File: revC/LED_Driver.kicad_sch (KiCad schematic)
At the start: 26 parts, among them Q1 BC857AW,115, Q2 BC857AW,115, Q3 BC857AW,115, Q602 BC857AW,115

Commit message: updated layout for fm.
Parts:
- removed Q1, Q3, Q602: BC857AW,115, Package_TO_SOT_SMD:SOT-323_SC-70, symbol backplane-rescue:Q_PNP_BEC-Device
- removed R1, R604: 0R, Resistor_SMD:R_0402_1005Metric, symbol backplane-rescue:R_US-Device
- removed R2, R3, R5: 4.7k, Resistor_SMD:R_0402_1005Metric, symbol backplane-rescue:R_US-Device
- added F1: 500mA, Fuse:Fuse_0603_1608Metric, symbol Device:Fuse_Small
- added R10, R11, R12, R13, R6, R7, R8, R9: 1k, Resistor_SMD:R_0402_1005Metric, symbol backplane-rescue:R_US-Device
- added R14, R15: 0R, Resistor_SMD:R_0402_1005Metric, symbol backplane-rescue:R_US-Device
- C201, C202, C203, C204, C205, C206, C207, C208: value 1uF -> 0.1uF; footprint Capacitor_SMD:C_0603_1608Metric -> Capacitor_SMD:C_0402_1005Metric
- D201, D202, D203, D204, D205, D206, D207, D208: value SK68XX-EC3210R -> SK6805-EC321R; footprint CubeSat_Backplane:SK6812-EC3210F -> CubeSat_Backplane:SK68xx-EC120x_ReverseMount; symbol CubeSat_Backplane:SK6812-EC321F -> CubeSat_Backplane:SK68xx
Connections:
- net DIN: now also R14.2
- net DIN_LED: now also R14.1, R6.2; no longer D208.3 (DIN)
- net DOUT: now also R15.1
- net DOUT_LED: now also R15.2
- net LED_PWR: now also F1.2; no longer Q2.2 (E)
- net at D201.3 (DIN): now also R13.2; no longer D202.2 (DOUT)
- net at D208.2 (DOUT): now also R7.1; no longer D207.3 (DIN)
- net at D202.3 (DIN): now also R12.2; no longer D203.2 (DOUT)
- net at D204.2 (DOUT): now also R11.1; no longer D203.3 (DIN)
- net at D204.3 (DIN): now also R10.2; no longer D205.2 (DOUT)
- net at D206.2 (DOUT): now also R9.1; no longer D205.3 (DIN)
- net at D207.2 (DOUT): now also R8.1; no longer D206.3 (DIN)
- new net: D208.3 (DIN), R6.1
- new net: F1.1, Q2.2 (E)
- new net: D206.3 (DIN), R8.2
- new net: D202.2 (DOUT), R13.1
- new net: D205.3 (DIN), R9.2
- new net: D205.2 (DOUT), R10.1
- new net: D203.2 (DOUT), R12.1
- new net: D207.3 (DIN), R7.2
- new net: D203.3 (DIN), R11.2
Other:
- note added: "LED power sw"
- note added: "Reverse-Mounted Addressable RGB LEDs (Neopixels)"
- note removed: "Din, Dout Protection Buffer"
- note removed: "LED power buffer"
- note removed: "Reverse-Mounted NeoPixels"
- moved on the sheet: C201, C202, C203, C204, C205, C206, C207, C208

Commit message: removed old files
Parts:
- renumbered F1 to F200, Q2 to Q200, R4 to R200, R14 to R201, R15 to R202, R13 to R203, R12 to R204, R11 to R205, R10 to R206, R9 to R207, R8 to R208, R7 to R209, R6 to R210
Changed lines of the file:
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@@
   (symbol (lib_id "backplane-rescue:Q_PNP_BEC-Device") (at 62.865 49.53 270) (mirror x) (unit 1)
     (in_bom yes) (on_board yes) (dnp no)
-    (property "Reference" "Q2" (at 70.485 50.165 90)
+    (property "Reference" "Q200" (at 70.485 50.165 90)
       (effects (font (size 1.27 1.27)))
     )
@@
       (project "backplane"
         (path "/83db9fc1-2403-4316-a6ed-41bf80609364/00000000-0000-0000-0000-000061b9d717"
-          (reference "Q2") (unit 1)
+          (reference "Q200") (unit 1)
         )
       )
@@
   (symbol (lib_name "R_US-Device_1") (lib_id "backplane-rescue:R_US-Device") (at 181.61 63.5 90) (unit 1)
     (in_bom yes) (on_board yes) (dnp no)
-    (property "Reference" "R8" (at 177.8 62.23 90)
+    (property "Reference" "R208" (at 177.8 62.23 90)
       (effects (font (size 1.27 1.27)))
     )
@@
       (project "backplane"
         (path "/83db9fc1-2403-4316-a6ed-41bf80609364/00000000-0000-0000-0000-000061b9d717"
-          (reference "R8") (unit 1)
+          (reference "R208") (unit 1)
         )
       )
@@
   (symbol (lib_name "R_US-Device_1") (lib_id "backplane-rescue:R_US-Device") (at 213.36 63.5 90) (unit 1)
     (in_bom yes) (on_board yes) (dnp no)
-    (property "Reference" "R9" (at 209.55 62.23 90)
+    (property "Reference" "R207" (at 209.55 62.23 90)
       (effects (font (size 1.27 1.27)))
     )
@@
       (project "backplane"
         (path "/83db9fc1-2403-4316-a6ed-41bf80609364/00000000-0000-0000-0000-000061b9d717"
-          (reference "R9") (unit 1)
+          (reference "R207") (unit 1)
         )
       )
@@
   (symbol (lib_name "R_US-Device_1") (lib_id "backplane-rescue:R_US-Device") (at 181.61 101.6 90) (unit 1)
     (in_bom yes) (on_board yes) (dnp no)
-    (property "Reference" "R12" (at 177.8 100.33 90)
+    (property "Reference" "R204" (at 177.8 100.33 90)
       (effects (font (size 1.27 1.27)))
     )
@@
       (project "backplane"
         (path "/83db9fc1-2403-4316-a6ed-41bf80609364/00000000-0000-0000-0000-000061b9d717"
-          (reference "R12") (unit 1)
+          (reference "R204") (unit 1)
         )
       )
@@
   (symbol (lib_id "backplane-rescue:R_US-Device") (at 55.88 74.93 270) (unit 1)
     (in_bom yes) (on_board yes) (dnp no)
-    (property "Reference" "R14" (at 55.88 69.723 90)
+    (property "Reference" "R201" (at 55.88 69.723 90)
       (effects (font (size 1.27 1.27)))
     )
@@
       (project "backplane"
         (path "/83db9fc1-2403-4316-a6ed-41bf80609364/00000000-0000-0000-0000-000061b9d717"
-          (reference "R14") (unit 1)
+          (reference "R201") (unit 1)
         )
       )
@@
   (symbol (lib_id "backplane-rescue:R_US-Device") (at 47.625 59.69 90) (unit 1)
     (in_bom yes) (on_board yes) (dnp no)
-    (property "Reference" "R4" (at 45.085 60.96 90)
+    (property "Reference" "R200" (at 45.085 60.96 90)
       (effects (font (size 1.27 1.27)) (justify left))
     )
@@
       (project "backplane"
         (path "/83db9fc1-2403-4316-a6ed-41bf80609364/00000000-0000-0000-0000-000061b9d717"
-          (reference "R4") (unit 1)
+          (reference "R200") (unit 1)
         )
       )
@@
   (symbol (lib_name "R_US-Device_1") (lib_id "backplane-rescue:R_US-Device") (at 149.86 63.5 90) (unit 1)
     (in_bom yes) (on_board yes) (dnp no)
-    (property "Reference" "R7" (at 146.05 62.23 90)
+    (property "Reference" "R209" (at 146.05 62.23 90)
       (effects (font (size 1.27 1.27)))
     )
@@
       (project "backplane"
         (path "/83db9fc1-2403-4316-a6ed-41bf80609364/00000000-0000-0000-0000-000061b9d717"
-          (reference "R7") (unit 1)
+          (reference "R209") (unit 1)
         )
       )
@@
   (symbol (lib_name "R_US-Device_1") (lib_id "backplane-rescue:R_US-Device") (at 149.86 101.6 90) (unit 1)
     (in_bom yes) (on_board yes) (dnp no)
-    (property "Reference" "R11" (at 146.05 100.33 90)
+    (property "Reference" "R205" (at 146.05 100.33 90)
       (effects (font (size 1.27 1.27)))
     )
@@
       (project "backplane"
         (path "/83db9fc1-2403-4316-a6ed-41bf80609364/00000000-0000-0000-0000-000061b9d717"
-          (reference "R11") (unit 1)
+          (reference "R205") (unit 1)
         )
       )
@@
   (symbol (lib_name "R_US-Device_1") (lib_id "backplane-rescue:R_US-Device") (at 113.03 63.5 270) (mirror x) (unit 1)
     (in_bom yes) (on_board yes) (dnp no)
-    (property "Reference" "R6" (at 116.84 62.23 90)
+    (property "Reference" "R210" (at 116.84 62.23 90)
       (effects (font (size 1.27 1.27)))
     )
@@
       (project "backplane"
         (path "/83db9fc1-2403-4316-a6ed-41bf80609364/00000000-0000-0000-0000-000061b9d717"
-          (reference "R6") (unit 1)
+          (reference "R210") (unit 1)
         )
       )
@@
   (symbol (lib_name "R_US-Device_1") (lib_id "backplane-rescue:R_US-Device") (at 213.36 101.6 90) (unit 1)
     (in_bom yes) (on_board yes) (dnp no)
-    (property "Reference" "R13" (at 209.55 100.33 90)
+    (property "Reference" "R203" (at 209.55 100.33 90)
       (effects (font (size 1.27 1.27)))
     )
@@
       (project "backplane"
         (path "/83db9fc1-2403-4316-a6ed-41bf80609364/00000000-0000-0000-0000-000061b9d717"
-          (reference "R13") (unit 1)
+          (reference "R203") (unit 1)
         )
       )
@@
   (symbol (lib_name "R_US-Device_1") (lib_id "backplane-rescue:R_US-Device") (at 119.38 101.6 90) (unit 1)
     (in_bom yes) (on_board yes) (dnp no)
-    (property "Reference" "R10" (at 115.57 100.33 90)
+    (property "Reference" "R206" (at 115.57 100.33 90)
       (effects (font (size 1.27 1.27)))
     )
@@
       (project "backplane"
         (path "/83db9fc1-2403-4316-a6ed-41bf80609364/00000000-0000-0000-0000-000061b9d717"
-          (reference "R10") (unit 1)
+          (reference "R206") (unit 1)
         )
       )
@@
   (symbol (lib_id "backplane-rescue:R_US-Device") (at 55.88 83.82 270) (unit 1)
     (in_bom yes) (on_board yes) (dnp no)
-    (property "Reference" "R15" (at 55.88 78.613 90)
+    (property "Reference" "R202" (at 55.88 78.613 90)
       (effects (font (size 1.27 1.27)))
     )
@@
       (project "backplane"
         (path "/83db9fc1-2403-4316-a6ed-41bf80609364/00000000-0000-0000-0000-000061b9d717"
-          (reference "R15") (unit 1)
+          (reference "R202") (unit 1)
         )
       )
@@
   (symbol (lib_id "Device:Fuse_Small") (at 48.26 46.99 180) (unit 1)
     (in_bom yes) (on_board yes) (dnp no)
-    (property "Reference" "F1" (at 49.53 49.53 90)
-      (effects (font (size 1.27 1.27)) (justify left))
-    )
-    (property "Value" "500mA" (at 49.53 40.005 90)
+    (property "Reference" "F200" (at 46.99 43.18 0)
+      (effects (font (size 1.27 1.27)) (justify left))
+    )
+    (property "Value" "500mA" (at 48.26 45.72 0)
       (effects (font (size 1.27 1.27)) (justify left))
     )
@@
       (project "backplane"
         (path "/83db9fc1-2403-4316-a6ed-41bf80609364/00000000-0000-0000-0000-000061b9d717"
-          (reference "F1") (unit 1)
-        )
-      )
+          (reference "F200") (unit 1)
+        )
+      )

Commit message: working post-review changes
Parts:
- removed F200: 500mA, Fuse:Fuse_0603_1608Metric, symbol Device:Fuse_Small
- removed Q200: BC857AW,115, Package_TO_SOT_SMD:SOT-323_SC-70, symbol backplane-rescue:Q_PNP_BEC-Device
- removed R200: 4.7k, Resistor_SMD:R_0402_1005Metric, symbol backplane-rescue:R_US-Device
- removed R201, R202: 0R, Resistor_SMD:R_0402_1005Metric, symbol backplane-rescue:R_US-Device
- D201, D202, D203, D204, D205, D206, D207, D208: Manufacturer Part Number 1 (none) -> SK6812-EC321R
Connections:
- net DIN_LED is gone; now on net DIN: R210.2
- net DOUT_LED is gone; now on net DOUT: D201.2 (DOUT)
- net LED_Vcc is gone; now on net LED_PWR: C201.1, C202.1, C203.1, C204.1, C205.1, C206.1, C207.1, C208.1, D201.4 (VDD), D202.4 (VDD), D203.4 (VDD), D204.4 (VDD), D205.4 (VDD), D206.4 (VDD), D207.4 (VDD), D208.4 (VDD)
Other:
- note removed: "LED power sw"

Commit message: revC commit
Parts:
- D201, D202, D203, D204, D205, D206, D207, D208: value SK6805-EC321R -> SK6805-EC321F; footprint CubeSat_Backplane:SK68xx-EC120x_ReverseMount -> SierraLobo:SK68xx-EC120x_ReverseMount
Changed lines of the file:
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@@
       (effects (font (size 1.27 1.27)))
     )
-    (property "Value" "SK6805-EC321R" (at 213.36 106.1593 0)
-      (effects (font (size 1.27 1.27)))
-    )
-    (property "Footprint" "CubeSat_Backplane:SK68xx-EC120x_ReverseMount" (at 228.6 109.22 0)
+    (property "Value" "SK6805-EC321F" (at 213.36 106.1593 0)
+      (effects (font (size 1.27 1.27)))
+    )
+    (property "Footprint" "SierraLobo:SK68xx-EC120x_ReverseMount" (at 228.6 109.22 0)
       (effects (font (size 1.27 1.27)) (justify left top) hide)
     )
@@
       (effects (font (size 1.27 1.27)))
     )
-    (property "Value" "SK6805-EC321R" (at 119.38 68.0593 0)
-      (effects (font (size 1.27 1.27)))
-    )
-    (property "Footprint" "CubeSat_Backplane:SK68xx-EC120x_ReverseMount" (at 134.62 71.12 0)
+    (property "Value" "SK6805-EC321F" (at 119.38 68.0593 0)
+      (effects (font (size 1.27 1.27)))
+    )
+    (property "Footprint" "SierraLobo:SK68xx-EC120x_ReverseMount" (at 134.62 71.12 0)
       (effects (font (size 1.27 1.27)) (justify left top) hide)
     )
@@
       (effects (font (size 1.27 1.27)))
     )
-    (property "Value" "SK6805-EC321R" (at 181.61 106.1593 0)
-      (effects (font (size 1.27 1.27)))
-    )
-    (property "Footprint" "CubeSat_Backplane:SK68xx-EC120x_ReverseMount" (at 196.85 109.22 0)
+    (property "Value" "SK6805-EC321F" (at 181.61 106.1593 0)
+      (effects (font (size 1.27 1.27)))
+    )
+    (property "Footprint" "SierraLobo:SK68xx-EC120x_ReverseMount" (at 196.85 109.22 0)
       (effects (font (size 1.27 1.27)) (justify left top) hide)
     )
@@
       (effects (font (size 1.27 1.27)))
     )
-    (property "Value" "SK6805-EC321R" (at 119.38 106.1593 0)
-      (effects (font (size 1.27 1.27)))
-    )
-    (property "Footprint" "CubeSat_Backplane:SK68xx-EC120x_ReverseMount" (at 134.62 109.22 0)
+    (property "Value" "SK6805-EC321F" (at 119.38 106.1593 0)
+      (effects (font (size 1.27 1.27)))
+    )
+    (property "Footprint" "SierraLobo:SK68xx-EC120x_ReverseMount" (at 134.62 109.22 0)
       (effects (font (size 1.27 1.27)) (justify left top) hide)
     )
@@
       (effects (font (size 1.27 1.27)))
     )
-    (property "Value" "SK6805-EC321R" (at 213.36 68.0593 0)
-      (effects (font (size 1.27 1.27)))
-    )
-    (property "Footprint" "CubeSat_Backplane:SK68xx-EC120x_ReverseMount" (at 228.6 71.12 0)
+    (property "Value" "SK6805-EC321F" (at 213.36 68.0593 0)
+      (effects (font (size 1.27 1.27)))
+    )
+    (property "Footprint" "SierraLobo:SK68xx-EC120x_ReverseMount" (at 228.6 71.12 0)
       (effects (font (size 1.27 1.27)) (justify left top) hide)
     )
@@
       (effects (font (size 1.27 1.27)))
     )
-    (property "Value" "SK6805-EC321R" (at 149.86 106.1593 0)
-      (effects (font (size 1.27 1.27)))
-    )
-    (property "Footprint" "CubeSat_Backplane:SK68xx-EC120x_ReverseMount" (at 165.1 109.22 0)
+    (property "Value" "SK6805-EC321F" (at 149.86 106.1593 0)
+      (effects (font (size 1.27 1.27)))
+    )
+    (property "Footprint" "SierraLobo:SK68xx-EC120x_ReverseMount" (at 165.1 109.22 0)
       (effects (font (size 1.27 1.27)) (justify left top) hide)
     )
@@
       (effects (font (size 1.27 1.27)))
     )
-    (property "Value" "SK6805-EC321R" (at 149.86 68.0593 0)
-      (effects (font (size 1.27 1.27)))
-    )
-    (property "Footprint" "CubeSat_Backplane:SK68xx-EC120x_ReverseMount" (at 165.1 71.12 0)
+    (property "Value" "SK6805-EC321F" (at 149.86 68.0593 0)
+      (effects (font (size 1.27 1.27)))
+    )
+    (property "Footprint" "SierraLobo:SK68xx-EC120x_ReverseMount" (at 165.1 71.12 0)
       (effects (font (size 1.27 1.27)) (justify left top) hide)
     )
@@
       (effects (font (size 1.27 1.27)))
     )
-    (property "Value" "SK6805-EC321R" (at 181.61 68.0593 0)
-      (effects (font (size 1.27 1.27)))
-    )
-    (property "Footprint" "CubeSat_Backplane:SK68xx-EC120x_ReverseMount" (at 196.85 71.12 0)
-      (effects (font (size 1.27 1.27)) (justify left top) hide)
-    )
+    (property "Value" "SK6805-EC321F" (at 181.61 68.0593 0)
+      (effects (font (size 1.27 1.27)))
+    )
+    (property "Footprint" "SierraLobo:SK68xx-EC120x_ReverseMount" (at 196.85 71.12 0)
+      (effects (font (size 1.27 1.27)) (justify left top) hide)
+    )

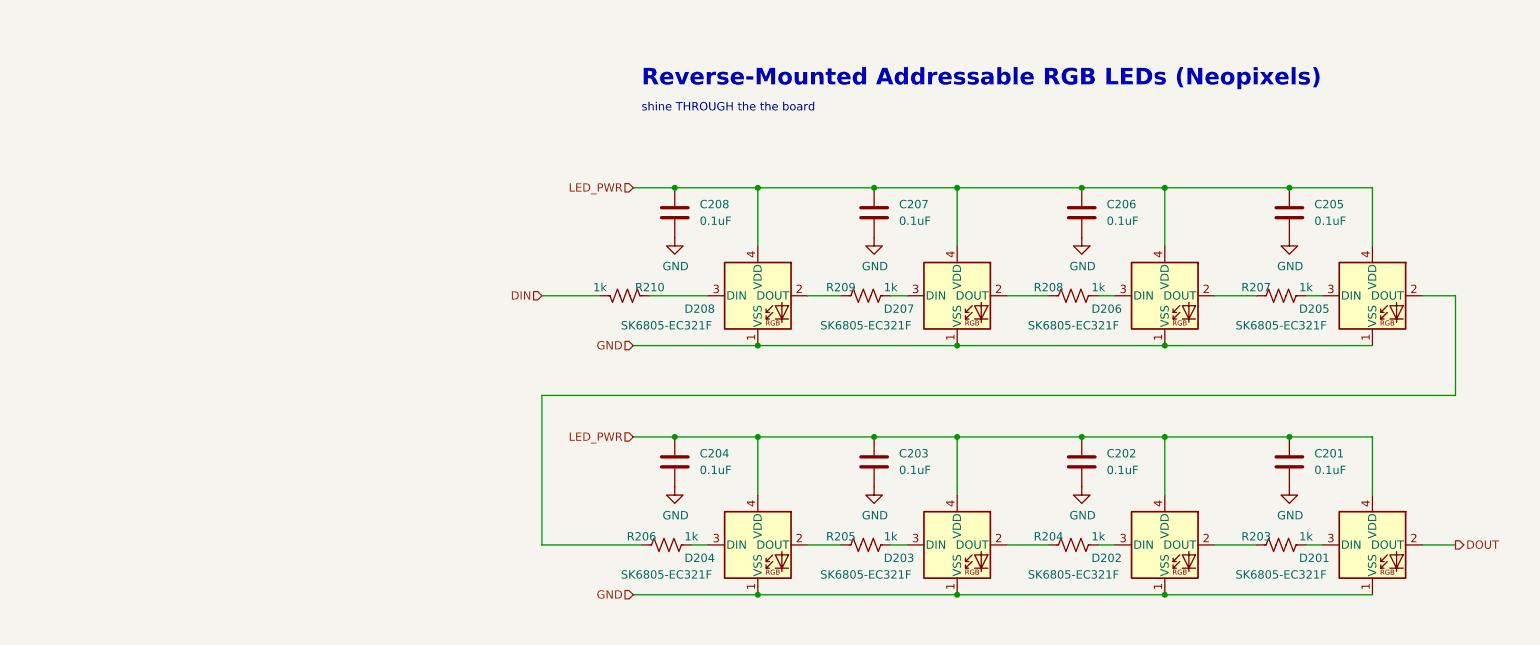
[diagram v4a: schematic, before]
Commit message: retrieved original revC, latest is now C1
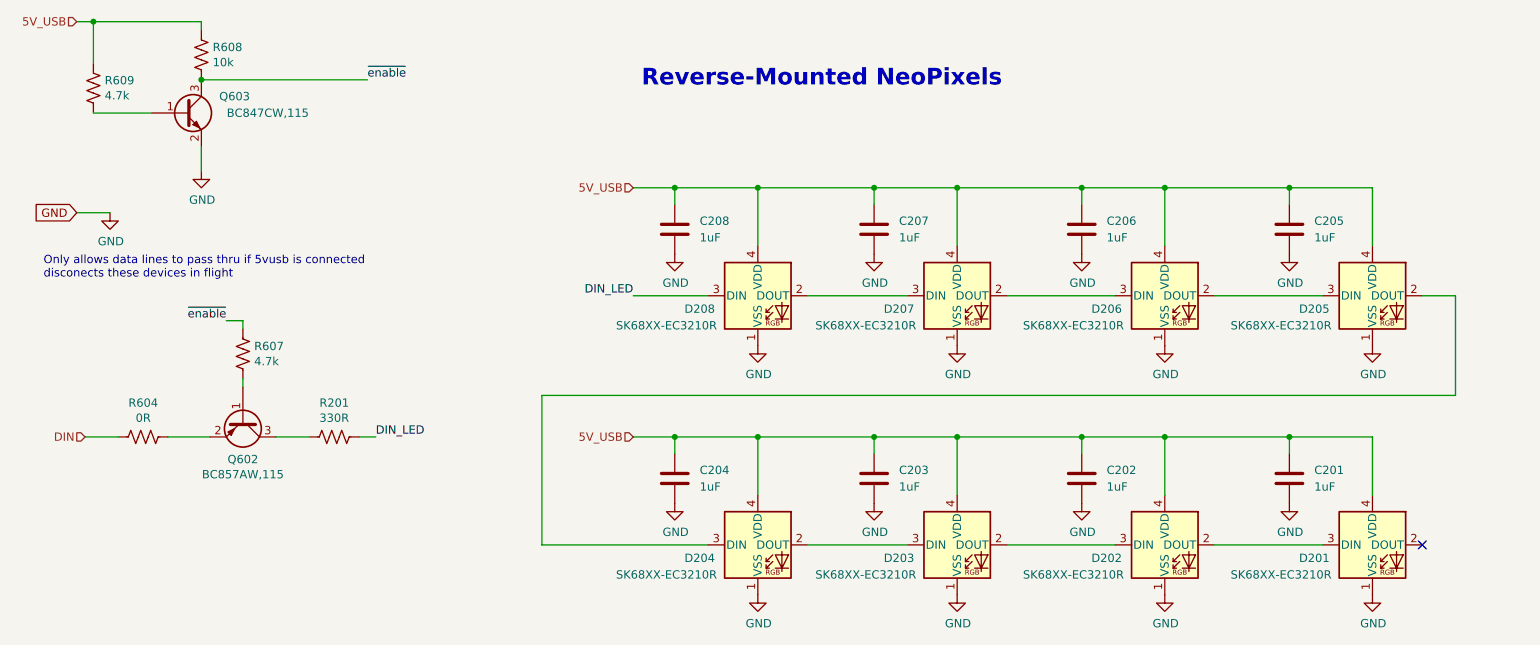
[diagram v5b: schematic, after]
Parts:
- removed R203, R204, R205, R206, R207, R208, R209, R210: 1k, Resistor_SMD:R_0402_1005Metric, symbol backplane-rescue:R_US-Device
- added Q602: BC857AW,115, Package_TO_SOT_SMD:SOT-323_SC-70, symbol backplane-rescue:Q_PNP_BEC-Device
- added Q603: BC847CW,115, Package_TO_SOT_SMD:SOT-323_SC-70, symbol backplane-rescue:Q_NPN_BEC-Device
- added R201: 330R, Resistor_SMD:R_0402_1005Metric, symbol backplane-rescue:R_US-Device
- added R604: 0R, Resistor_SMD:R_0402_1005Metric, symbol backplane-rescue:R_US-Device
- added R607, R609: 4.7k, Resistor_SMD:R_0402_1005Metric, symbol backplane-rescue:R_US-Device
- added R608: 10k, Resistor_SMD:R_0402_1005Metric, symbol backplane-rescue:R_US-Device
- C201, C202, C203, C204, C205, C206, C207, C208: value 0.1uF -> 1uF; footprint Capacitor_SMD:C_0402_1005Metric -> Capacitor_SMD:C_0603_1608Metric
- D201, D202, D203, D204, D205, D206, D207, D208: value SK6805-EC321F -> SK68XX-EC3210R; footprint SierraLobo:SK68xx-EC120x_ReverseMount -> CubeSat_Backplane:SK6812-EC3210F; symbol CubeSat_Backplane:SK68xx -> CubeSat_Backplane:SK6812-EC321F; Manufacturer Part Number 1 SK6812-EC321R -> (none)
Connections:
- net DIN: now also R604.2
- net GND: now also Q603.2 (E)
- net at D201.3 (DIN): now also D202.2 (DOUT)
- net at D208.2 (DOUT): now also D207.3 (DIN)
- net DIN_LED: now reaches D208.3 (DIN)
- net DIN_LED: now also R201.1
- net at D207.2 (DOUT): now also D206.3 (DIN)
- net at D202.3 (DIN): now also D203.2 (DOUT)
- net at D204.2 (DOUT): now also D203.3 (DIN)
- net at D204.3 (DIN): now also D205.2 (DOUT)
- net at D206.2 (DOUT): now also D205.3 (DIN)
- net DOUT: no longer names the net of D201.2 (DOUT)
- net LED_PWR renamed 5V_USB
- net 5V_USB: now also R608.1, R609.1
- new net: Q603.1 (B), R609.2
- new net: Q602.2 (E), R604.1
- new net: Q602.1 (B), R607.2
- new net: Q602.3 (C), R201.2
- new net ~{enable}: Q603.3 (C), R607.1, R608.2
- no-connect marks 0 -> 1
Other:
- note added: "Only allows data lines to pass thru if 5vusb is connected disconects these devices in flight"
- note added: "Reverse-Mounted NeoPixels"
- note removed: "Reverse-Mounted Addressable RGB LEDs (Neopixels)"
- note removed: "shine THROUGH the the board"
- moved on the sheet: C201, C202, C203, C204, C205, C206, C207, C208
